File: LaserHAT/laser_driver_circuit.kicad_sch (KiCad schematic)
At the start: 28 parts, among them J1 Conn_01x06_Pin, Q1 DMG2302U, Q2 BSS138DW, U1 TLV2371DBV

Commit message: Updates with lots of manual work
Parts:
- removed C1, C2: 100nF, Capacitor_SMD:C_0402_1005Metric, symbol Device:C
- removed C_IN1: 10µF 10V, Capacitor_SMD:C_0805_2012Metric, symbol Device:C
- removed C_IN2: 100nF 10V, Capacitor_SMD:C_0402_1005Metric, symbol Device:C
- removed C_OUT1: 10µF 16V, Capacitor_SMD:C_0805_2012Metric, symbol Device:C
- removed C_OUT2: 100nF 16V, Capacitor_SMD:C_0402_1005Metric, symbol Device:C
- removed D_BOOST: SS14, Diode_SMD:D_SMA, symbol Diode:SS14
- removed J1: Conn_01x06_Pin, Connector_PinHeader_2.54mm:PinHeader_1x06_P2.54mm_Vertical, symbol Connector:Conn_01x06_Pin
- removed LD1: D_Laser_Photo_NType, Connector_PinHeader_2.54mm:PinHeader_1x03_P2.54mm_Vertical, symbol Device:D_Laser_Photo_NType
- removed R_EN: 100k, Resistor_SMD:R_0402_1005Metric, symbol Device:R
- removed R_FB1: 187k 1%, Resistor_SMD:R_0402_1005Metric, symbol Device:R
- removed R_FB2: 10k 1%, Resistor_SMD:R_0402_1005Metric, symbol Device:R
- removed U_BOOST: MT3608, Package_TO_SOT_SMD:SOT-23-6_Handsoldering, symbol Regulator_Switching:MT3608
- added C10: 100nF 16V, Capacitor_SMD:C_0402_1005Metric, symbol Device:C_Small
- added C7: 100nF 10V, Capacitor_SMD:C_0402_1005Metric, symbol Device:C_Small
- added C8: 22µF 10V, Capacitor_SMD:C_1206_3216Metric, symbol Device:C_Small
- added C9: 22µF 16V, Capacitor_SMD:C_1206_3216Metric, symbol Device:C_Small
- added D1: SS14, Diode_SMD:D_SMA, symbol Device:D
- added J2: Conn_02x02_Counter_Clockwise, Connector_PinHeader_2.54mm:PinHeader_2x02_P2.54mm_Vertical, symbol Connector_Generic:Conn_02x02_Counter_Clockwise
- added J3: Conn_01x03_Pin, symbol Connector:Conn_01x03_Pin
- added J4: Jumper for 4-terminal diode configuration, symbol Connector:Conn_01x02_Pin
- added JP2, JP3: SolderJumper_2_Open, Jumper:SolderJumper-2_P1.3mm_Open_TrianglePad1.0x1.5mm, symbol Jumper:SolderJumper_2_Open
- added R5: 187K 1%, Resistor_SMD:R_0402_1005Metric, symbol Device:R
- added R6: 10K 1%, Resistor_SMD:R_0402_1005Metric, symbol Device:R
- added R7: 140 1%, Resistor_SMD:R_0402_1005Metric, symbol Device:R
- added U2: MT3608, Package_TO_SOT_SMD:SOT-23-6, symbol Regulator_Switching:MT3608
- C11: renamed from C3; symbol Device:C -> Device:C_Small
- L1: value 22µH -> L; footprint Inductor_SMD:L_Bourns_SRR1260 -> (none)
- Q1: renamed from Q2; LCSC Part # (none) -> C919584
- Q2: renamed from Q1; value DMG2302U -> DMN2056U; LCSC Part # (none) -> C332302
- R12: renamed from R2; value 10k -> 4.7k
- U3: renamed from U1; LCSC Part # (none) -> C55940
- renumbered D1 to D2, D2 to D3, D3 to D4, JP1 to JP5, JP2 to JP6, Q2 to Q1, R1 to R11, R4 to R9, R3 to Rsense
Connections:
- net SwitchedLaserDrive is gone; now on net LaserDrive: Q1.1 (S), Q1.4 (S), Q2.3 (D)
- net BOOST_EN: now also U2.4 (EN)
- net LaserDrive: no longer Q1.3 (D)
- net at R11.2, R12.1: now also J2.4 (PD_Anode)
- net +LASER_V renamed GND
- net GND: now also C10.2, C7.2, C8.2, C9.2, R6.2, U2.2 (GND); no longer R9.1, U3.5 (V+)
- net ADC renamed DIODE_ADC
- net BOOST_OUT_SW: no longer names the net of L1.2
- net BOOST_OUT_SW: now also D1.2 (A), U2.1 (SW)
- net BOOST_SW renamed V_LASER_BOOST_IN
- net V_LASER_BOOST_IN: now also C7.1, C8.1, J3.3 (Pin_3), U2.5 (IN)
- net VREF renamed LASER_VREF
- new net: J2.2 (LD_Cathode), Q1.3 (D)
- new net: J2.3 (PD_Cathode), J4.1 (Pin_1)
- new net: D1.1 (K), J3.1 (Pin_1), R5.1, R7.1
- new net: JP2.2 (B), R5.2
- new net: JP2.1 (A), JP3.1 (A), R6.1, U2.3 (FB)
- new net: JP3.2 (B), R7.2
- new net LASER_V: C10.1, C9.1, J2.1 (LD_Anode), J3.2 (Pin_2), J4.2 (Pin_2), R9.1, U3.5 (V+)
- no-connect marks 1 -> 0
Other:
- note added: "Choose for 12V or 9V"
- note added: "Jumper to bypass for just 5V"
- note added: "Supply: +12V (analog), +3V3 (MCU logic)"
- note removed: "Supply: +5V (analog), +3V3 (MCU logic)"
- moved on the sheet: C11, D2, D3, D4, JP5, JP6, Q1A, Q1B, Q2, R11, R12, R9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

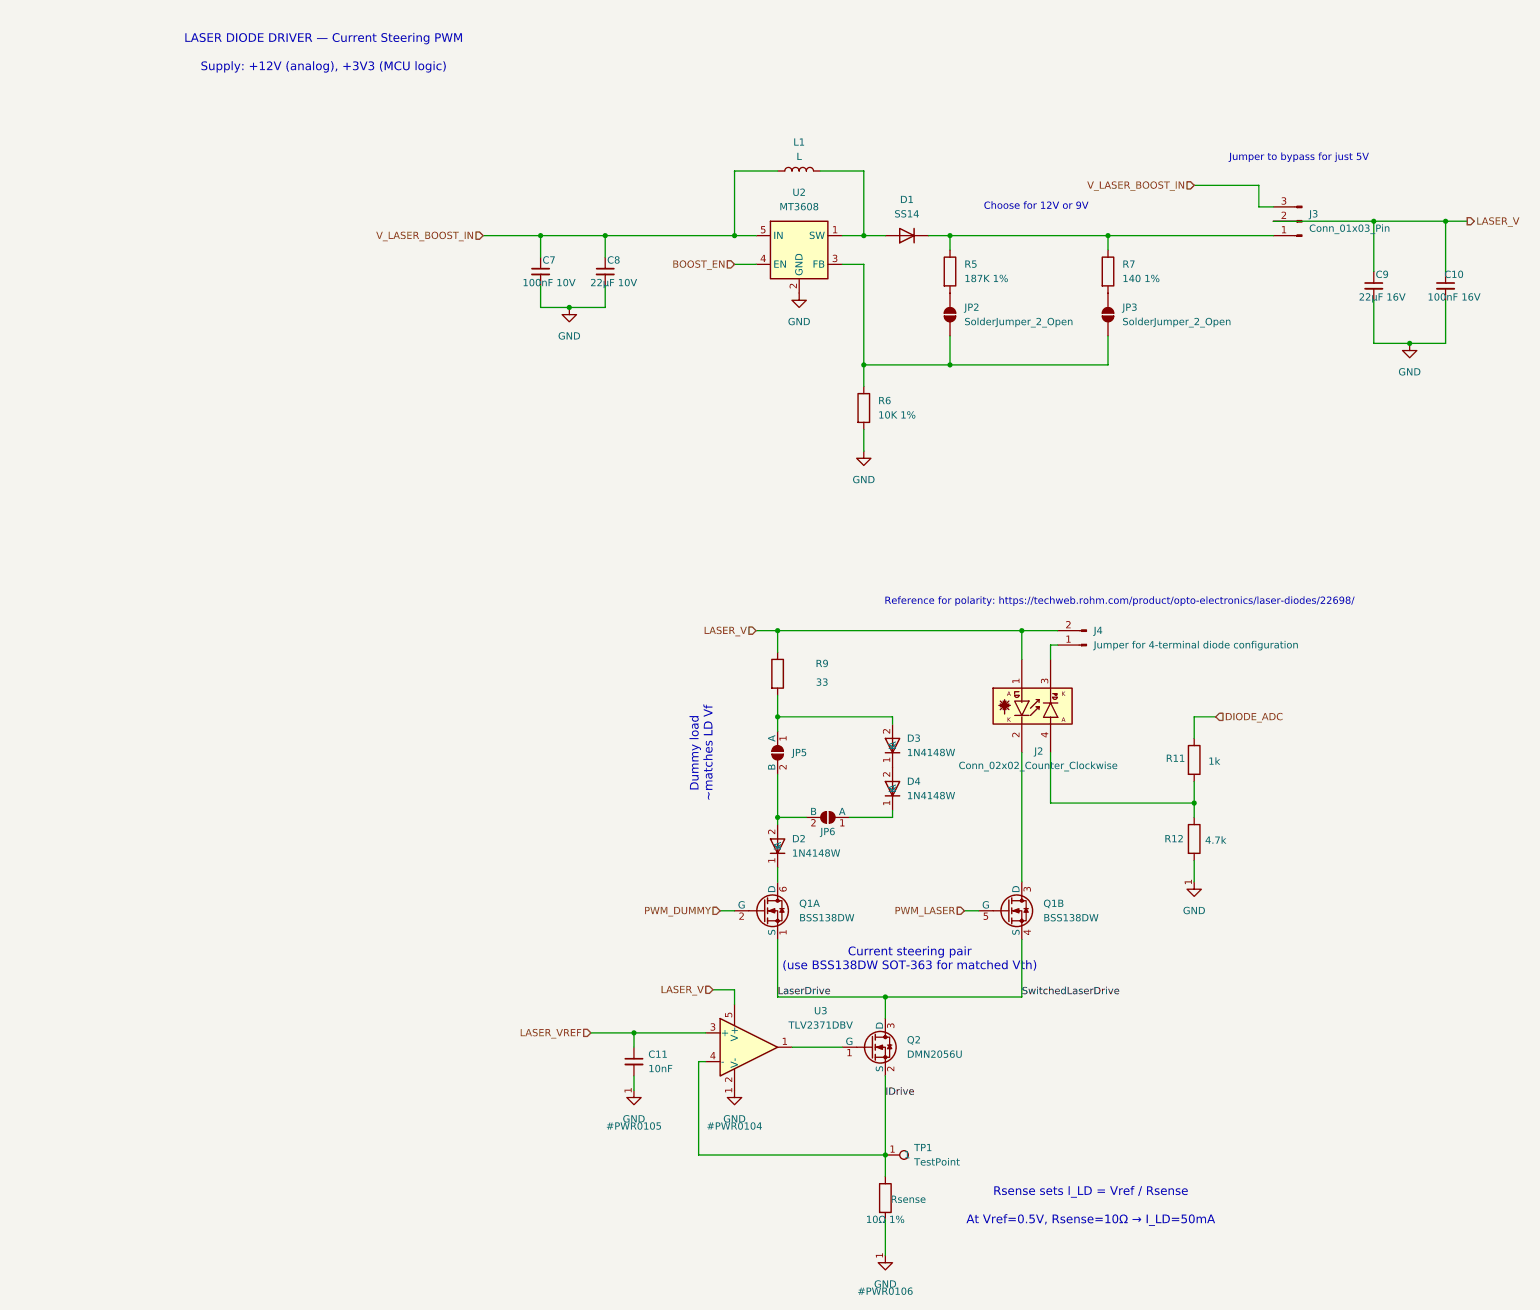
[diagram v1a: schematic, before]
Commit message: Updates to design, finalized PCB layout
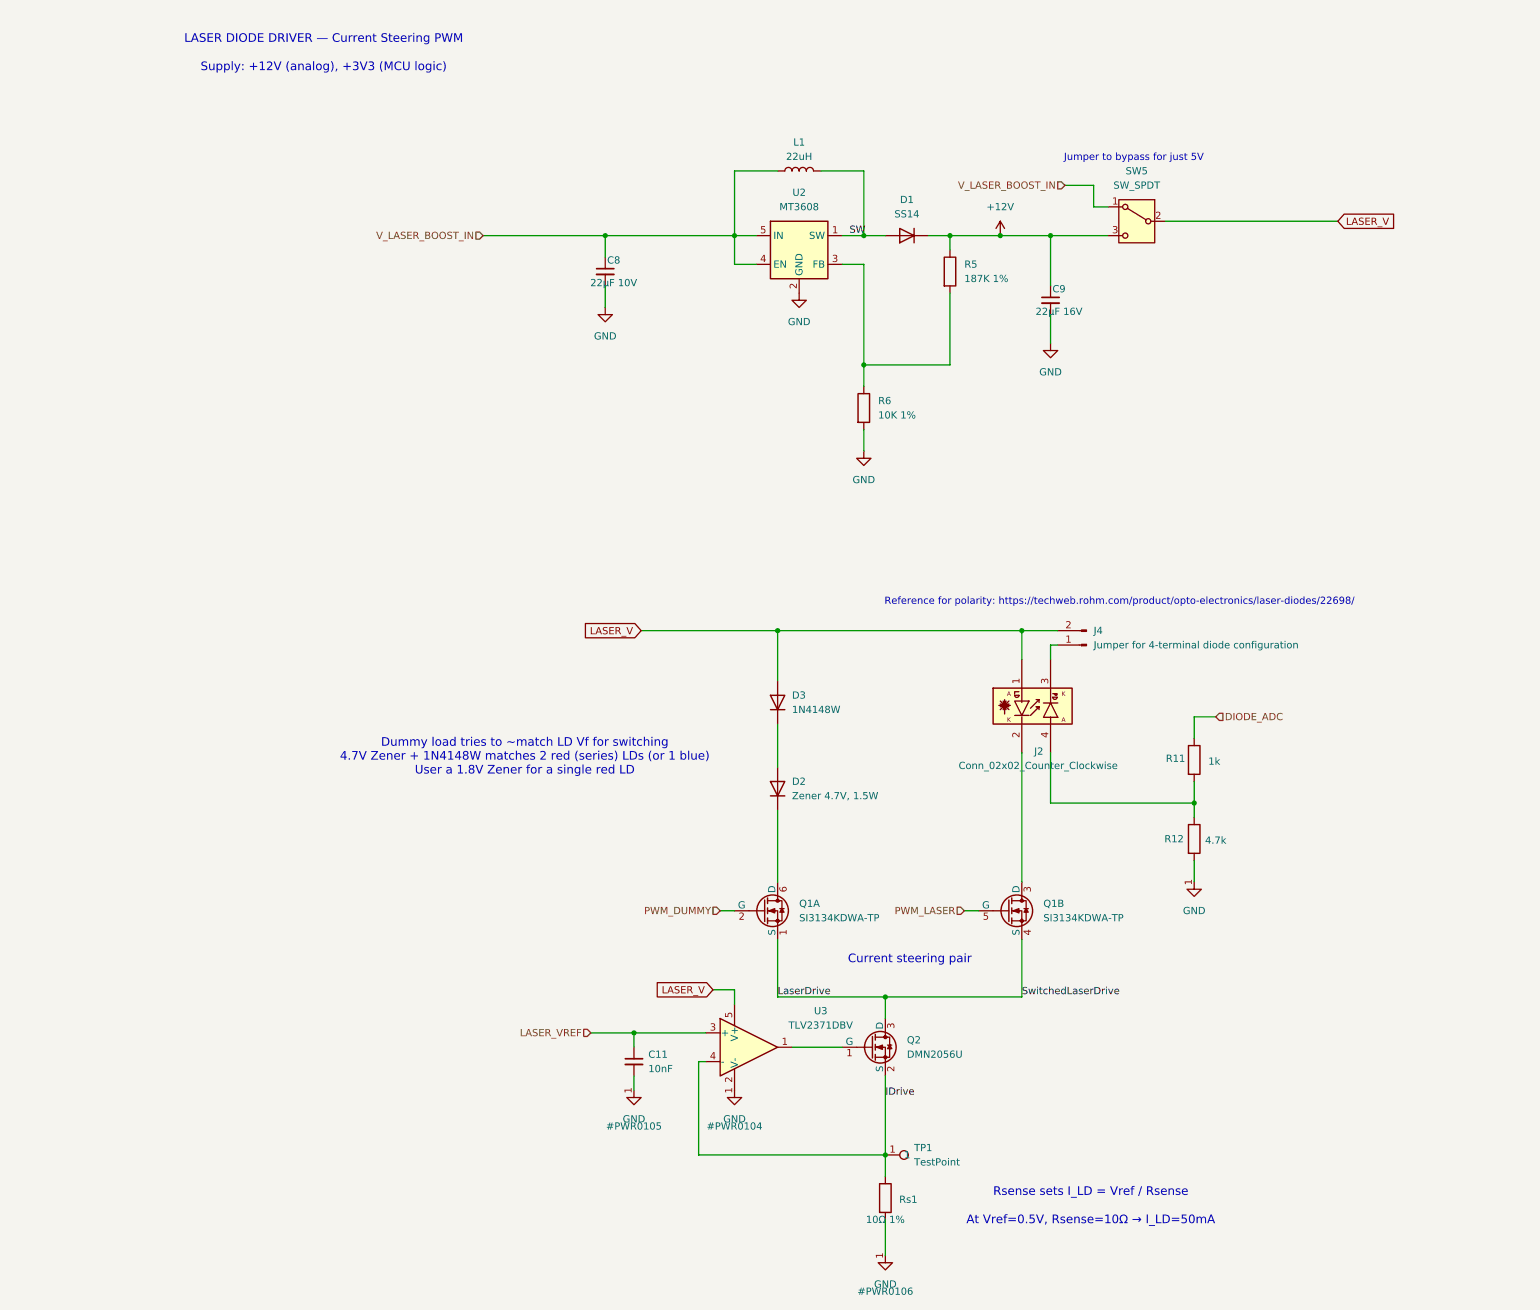
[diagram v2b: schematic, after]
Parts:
- removed C10: 100nF 16V, Capacitor_SMD:C_0402_1005Metric, symbol Device:C_Small
- removed C7: 100nF 10V, Capacitor_SMD:C_0402_1005Metric, symbol Device:C_Small
- removed D4: 1N4148W, Diode_SMD:D_SOD-123, symbol Diode:1N4148W
- removed J3: Conn_01x03_Pin, symbol Connector:Conn_01x03_Pin
- removed JP2, JP3: SolderJumper_2_Open, Jumper:SolderJumper-2_P1.3mm_Open_TrianglePad1.0x1.5mm, symbol Jumper:SolderJumper_2_Open
- removed JP5, JP6: ~, Jumper:SolderJumper-2_P1.3mm_Open_TrianglePad1.0x1.5mm, symbol Jumper:SolderJumper_2_Open
- removed R7: 140 1%, Resistor_SMD:R_0402_1005Metric, symbol Device:R
- removed R9: 33, Resistor_SMD:R_0402_1005Metric, symbol Device:R
- added SW5: SW_SPDT, ELEC327-Kicad:SW_EG1270, symbol Switch:SW_SPDT
- D1: footprint Diode_SMD:D_SMA -> Diode_SMD:D_SOD-123F; LCSC Part # C83852 -> C894423
- D2: value 1N4148W -> Zener 4.7V, 1.5W; footprint Diode_SMD:D_SOD-123 -> Diode_SMD:D_SMA; LCSC Part # (none) -> C5161049
- D3: footprint Diode_SMD:D_SOD-123 -> Footprints:D_SOD-323F; LCSC Part # (none) -> C119617
- J4: footprint (none) -> Connector_PinHeader_2.54mm:PinHeader_1x02_P2.54mm_Vertical
- L1: value L -> 22uH; footprint (none) -> Inductor_SMD:L_APV_ANR6045; LCSC Part # (none) -> C7427158
- Q1: value BSS138DW -> SI3134KDWA-TP; LCSC Part # (none) -> C3290118
- Q1: value BSS138DW -> SI3134KDWA-TP; LCSC Part # C919584 -> C3290118
- Rs1: renamed from Rsense; footprint Resistor_SMD:R_0402_1005Metric -> Resistor_SMD:R_1206_3216Metric; LCSC Part # (none) -> C42460620
- TP1: footprint Connector_PinHeader_2.54mm:PinHeader_1x01_P2.54mm_Vertical -> TestPoint:TestPoint_Pad_D1.5mm
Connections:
- net BOOST_EN is gone; now on net V_LASER_BOOST_IN: U2.4 (EN)
- net LASER_V: now also D3.2 (A), SW5.2 (B); no longer C9.1
- net V_LASER_BOOST_IN: now also SW5.1 (A)
- net at D3.1 (K): now also D2.2 (A)
- net SW: now reaches D1.2 (A), L1.2, U2.1 (SW)
- net +12V: now reaches D1.1 (K), R5.1
- net +12V: now also C9.1, SW5.3 (C)
- net at R5.2: now also R6.1, U2.3 (FB)
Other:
- note added: "Current steering pair"
- note added: "Dummy load tries to ~match LD Vf for switching 4.7V Zener + 1N4148W matches 2 red (series) LDs (or 1 blue) User a 1.8V Zener for a single red LD"
- note removed: "Choose for 12V or 9V"
- note removed: "Current steering pair (use BSS138DW SOT-363 for matched Vth)"
- note removed: "Dummy load ~matches LD Vf"
- moved on the sheet: C9

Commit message: Updated project for manufacturing. Should merge branch if/when we get back a working product
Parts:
- C11: LCSC Part # (none) -> C15195
- C8: value 22µF 10V -> 22µF 16V; LCSC Part # (none) -> C12891
- C9: LCSC Part # (none) -> C12891
- J2, J4: now not fitted
- R11: value 1k -> 1k 0.1%; LCSC Part # (none) -> C843869
- R12: LCSC Part # (none) -> C25900
- R5: value 187K 1% -> 187k 1%; LCSC Part # (none) -> C844101
- R6: value 10K 1% -> 10k; LCSC Part # (none) -> C25744
- SW5: footprint ELEC327-Kicad:SW_EG1270 -> Button_Switch_SMD:SW_SPDT_PCM12; LCSC Part # (none) -> C221841
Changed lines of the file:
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@@
 			)
 		)
-		(property "Description" ""
+		(property "Description" "100mW 4.7kΩ 50V Thin Film Resistor ±50ppm/℃ ±1% 0402 Chip Resistor - Surface Mount RoHS"
 			(at 200.66 162.56 0)
 			(effects
@@
 			)
 		)
-		(property "LCSC Part #" ""
+		(property "LCSC Part #" "C25900"
 			(at 200.66 162.56 0)
 			(effects
@@
 		(in_bom yes)
 		(on_board yes)
-		(dnp no)
+		(dnp yes)
 		(fields_autoplaced yes)
 		(property "Reference" "J4"
@@
 			)
 		)
-		(property "Description" "Inductor"
+		(property "Description" "2A 22uH ±20% 2.2A Magnetic Shielded Inductor SMD,6x6mm Fixed Inductors RoHS"
 			(at 130.81 44.45 0)
 			(effects
@@
 			)
 		)
-		(property "Description" "Unpolarized capacitor, small symbol"
+		(property "Description" "22uF ±10% 16V Ceramic Capacitor X5R 1206"
 			(at 175.26 67.31 0)
 			(effects
@@
 			)
 		)
-		(property "LCSC Part #" ""
+		(property "LCSC Part #" "C12891"
 			(at 175.26 67.31 0)
 			(effects
@@
 			)
 		)
-		(property "Value" "187K 1%"
+		(property "Value" "187k 1%"
 			(at 160.02 63.4999 0)
 			(effects
@@
 			)
 		)
-		(property "Description" "Resistor"
+		(property "Description" "62.5mW 187kΩ Thick Film Resistor ±100ppm/℃ ±1% 0402 Chip Resistor - Surface Mount RoHS"
 			(at 157.48 62.23 0)
 			(effects
@@
 			)
 		)
-		(property "LCSC Part #" ""
+		(property "LCSC Part #" "C844101"
 			(at 157.48 62.23 0)
 			(effects
@@
 		(in_bom yes)
 		(on_board yes)
-		(dnp no)
+		(dnp yes)
 		(property "Reference" "J2"
 			(at 173.99 147.066 0)
@@
 			)
 		)
-		(property "Description" "Unpolarized capacitor, small symbol"
+		(property "Description" "10nF ±10% 50V Ceramic Capacitor X7R 0402"
 			(at 101.6 201.93 0)
 			(effects
@@
 			)
 		)
-		(property "LCSC Part #" ""
+		(property "LCSC Part #" "C15195"
 			(at 101.6 201.93 0)
 			(effects
@@
 			)
 		)
-		(property "Value" "1k"
+		(property "Value" "1k 0.1%"
 			(at 204.216 148.844 0)
 			(effects
@@
 			)
 		)
-		(property "Description" ""
+		(property "Description" "100mW 1kΩ Thin Film Resistor ±25ppm/℃ ±0.1% 0402 Chip Resistor - Surface Mount RoHS"
 			(at 200.66 148.59 0)
 			(effects
@@
 			)
 		)
-		(property "LCSC Part #" ""
+		(property "LCSC Part #" "C843869"
 			(at 200.66 148.59 0)
 			(effects
@@
 			)
 		)
-		(property "Value" "10K 1%"
+		(property "Value" "10k"
 			(at 144.78 87.6299 0)
 			(effects
@@
 			)
 		)
-		(property "Description" "Resistor"
+		(property "Description" "200mW 10kΩ Thick Film Resistor ±100ppm/℃ ±1% 0402 Chip Resistor - Surface Mount RoHS"
 			(at 142.24 86.36 0)
 			(effects
@@
 			)
 		)
-		(property "LCSC Part #" ""
+		(property "LCSC Part #" "C25744"
 			(at 142.24 86.36 0)
 			(effects
@@
 			)
 		)
-		(property "Value" "22µF 10V"
+		(property "Value" "22µF 16V"
 			(at 98.02 64.23 0)
 			(effects
@@
 			)
 		)
-		(property "Description" "Unpolarized capacitor, small symbol"
+		(property "Description" "22uF ±10% 16V Ceramic Capacitor X5R 1206"
 			(at 96.52 62.23 0)
 			(effects
@@
 			)
 		)
-		(property "LCSC Part #" ""
+		(property "LCSC Part #" "C12891"
 			(at 96.52 62.23 0)
 			(effects
@@
 			)
 		)
-		(property "LCSC Part #" ""
-			(at 146.05 218.44 90)
-			(effects
-				(font
-					(size 1.27 1.27)
-				)
-				(hide yes)
-			)
-		)
 		(pin "1"
 		)
@@
 			)
 		)
-		(property "Footprint" "ELEC327-Kicad:SW_EG1270"
+		(property "Footprint" "Button_Switch_SMD:SW_SPDT_PCM12"
 			(at 190.5 53.34 0)
 			(effects
@@
 			(at 190.5 53.34 0)
 			(effects
+				(font
+					(size 1.27 1.27)
+				)
+				(hide yes)
+			)
+		)
+		(property "LCSC Part #" "C221841"
+			(at 190.5 53.34 0)
+			(effects
